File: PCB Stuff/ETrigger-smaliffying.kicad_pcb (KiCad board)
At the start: 2 copper layers, 33.7 x 27.5 mm, 53 parts, among them IC1 ATTINY85-S, P1 CONN_01X04, Q1 S8550, Q2 S8550, U1 AP1117, U4 LM321C

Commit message: Wow....
No comment I need to slow down a bit...and probably go to bed...
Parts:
- removed the REF** at (152.5, 90.8)
- removed the REF** at (151.5, 90.8)
- renumbered U4 to LM321, Q1 to S8550, Q2 to S8550, U1 to xx1117
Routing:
- net VCC_ICSP: track 140.6 -> 132.7 mm
- net GND_ICSP: track 56.4 -> 57.8 mm
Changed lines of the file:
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@@
 (kicad_pcb (version 4) (host pcbnew 4.0.5)
   (general
-    (links 82)
+    (links 0)
     (no_connects 0)
     (area 136.830709 82.456999 170.595002 111.507001)
     (thickness 1.6)
     (drawings 248)
-    (tracks 319)
+    (tracks 318)
     (zones 0)
-    (modules 53)
+    (modules 51)
     (nets 17)
   )
   (page A4)
   (layers
-    (0 F.Cu signal)
+    (0 F.Cu signal hide)
     (31 B.Cu signal)
     (32 B.Adhes user)
@@
     (visible_elements 7FFEF6FF)
     (pcbplotparams
-      (layerselection 0x00030_80000001)
-      (usegerberextensions false)
+      (layerselection 0x011f0_80000001)
+      (usegerberextensions true)
       (excludeedgelayer true)
       (linewidth 0.100000)
@@
       (outputformat 1)
       (mirror false)
-      (drillshape 1)
+      (drillshape 0)
       (scaleselection 1)
-      (outputdirectory ""))
+      (outputdirectory "ETrig Board/"))
   )
   (net 0 "")
@@
     (add_net VCC_ICSP)
   )
+  (module TO_SOT_Packages_SMD:SOT-223 (layer F.Cu)
+    (at 150.8379 89.0647 270)
+    (descr "module CMS SOT223 4 pins")
+    (tags "CMS SOT")
+    (attr smd)
+    (fp_text reference xx1117 (at 3.15 -3.5433 360) (layer F.SilkS)
+      (effects (font (size 0.5 0.5) (thickness 0.1)))
+    )
+    (fp_text value AP1117 (at 0 4.5 270) (layer F.Fab)
+      (effects (font (size 1 1) (thickness 0.15)))
+    )
+    (fp_text user %R (at 0 0 270) (layer F.Fab)
+      (effects (font (size 0.8 0.8) (thickness 0.12)))
+    )
+    (fp_line (start -1.85 -2.3) (end -0.8 -3.35) (layer F.Fab) (width 0.1))
+    (fp_line (start 4.4 -3.6) (end -4.4 -3.6) (layer F.CrtYd) (width 0.05))
+    (fp_line (start 4.4 3.6) (end 4.4 -3.6) (layer F.CrtYd) (width 0.05))
+    (fp_line (start -4.4 3.6) (end 4.4 3.6) (layer F.CrtYd) (width 0.05))
+    (fp_line (start -4.4 -3.6) (end -4.4 3.6) (layer F.CrtYd) (width 0.05))
+    (fp_line (start -1.85 -2.3) (end -1.85 3.35) (layer F.Fab) (width 0.1))
+    (fp_line (start -0.8 -3.35) (end 1.85 -3.35) (layer F.Fab) (width 0.1))
+    (fp_line (start -1.85 3.35) (end 1.85 3.35) (layer F.Fab) (width 0.1))
+    (fp_line (start 1.85 -3.35) (end 1.85 3.35) (layer F.Fab) (width 0.1))
+    (pad 4 smd rect (at 3.15 0 270) (size 2 3.8) (layers F.Cu F.Paste F.Mask)
+      (net 1 VCC_ICSP) (zone_connect 2))
+    (pad 2 smd rect (at -3.15 0 270) (size 2 1.5) (layers F.Cu F.Paste F.Mask)
+      (net 1 VCC_ICSP))
+    (pad 3 smd rect (at -3.15 2.3 270) (size 2 1.5) (layers F.Cu F.Paste F.Mask)
+      (net 4 +BATT))
+    (pad 1 smd rect (at -3.15 -2.3 270) (size 2 1.5) (layers F.Cu F.Paste F.Mask)
+      (net 5 GND_ICSP))
+    (model ${KISYS3DMOD}/TO_SOT_Packages_SMD.3dshapes/SOT-223.wrl
+      (at (xyz 0 0 0))
+      (scale (xyz 0.5 0.5 0.5))
+      (rotate (xyz 0 0 90))
+    )
+  )
   (module Capacitors_SMD:C_0805_HandSoldering (layer F.Cu)
     (at 169.01 97.39 270)
@@
   )
   (module "Via 2" (layer F.Cu)
-    (at 152.47 90.78)
-    (clearance 0.00001)
-    (zone_connect 2)
-    (fp_text reference REF** (at 0.127 4.699) (layer F.SilkS) hide
-      (effects (font (size 0.127 0.127) (thickness 0.03175)))
-    )
-    (fp_text value "Via 2" (at -0.127 -5.969) (layer F.Fab) hide
-      (effects (font (size 0.127 0.127) (thickness 0.03175)))
-    )
-    (pad 1 thru_hole circle (at 0 0) (size 0.6 0.6) (drill 0.3) (layers *.Cu)
-      (net 1 VCC_ICSP) (zone_connect 2))
-  )
-  (module "Via 2" (layer F.Cu)
-    (at 151.47 90.78)
-    (clearance 0.00001)
-    (zone_connect 2)
-    (fp_text reference REF** (at 0.127 4.699) (layer F.SilkS) hide
-      (effects (font (size 0.127 0.127) (thickness 0.03175)))
-    )
-    (fp_text value "Via 2" (at -0.127 -5.969) (layer F.Fab) hide
-      (effects (font (size 0.127 0.127) (thickness 0.03175)))
-    )
-    (pad 1 thru_hole circle (at 0 0) (size 0.6 0.6) (drill 0.3) (layers *.Cu)
-      (net 1 VCC_ICSP) (zone_connect 2))
-  )
-  (module "Via 2" (layer F.Cu)
     (at 152.47 90.03)
     (clearance 0.00001)
@@
     (pad 1 thru_hole circle (at 0 0) (size 0.6 0.6) (drill 0.3) (layers *.Cu)
       (net 5 GND_ICSP) (zone_connect 2))
-  )
-  (module TO_SOT_Packages_SMD:SOT-223 (layer F.Cu)
-    (at 150.8379 89.0774 270)
-    (descr "module CMS SOT223 4 pins")
-    (tags "CMS SOT")
-    (attr smd)
-    (fp_text reference U1 (at 3.0611 -2.9591 360) (layer F.SilkS)
-      (effects (font (size 1 1) (thickness 0.15)))
-    )
-    (fp_text value AP1117 (at 0 4.5 270) (layer F.Fab)
-      (effects (font (size 1 1) (thickness 0.15)))
-    )
-    (fp_text user %R (at 0 0 270) (layer F.Fab)
-      (effects (font (size 0.8 0.8) (thickness 0.12)))
-    )
-    (fp_line (start -1.85 -2.3) (end -0.8 -3.35) (layer F.Fab) (width 0.1))
-    (fp_line (start 4.4 -3.6) (end -4.4 -3.6) (layer F.CrtYd) (width 0.05))
-    (fp_line (start 4.4 3.6) (end 4.4 -3.6) (layer F.CrtYd) (width 0.05))
-    (fp_line (start -4.4 3.6) (end 4.4 3.6) (layer F.CrtYd) (width 0.05))
-    (fp_line (start -4.4 -3.6) (end -4.4 3.6) (layer F.CrtYd) (width 0.05))
-    (fp_line (start -1.85 -2.3) (end -1.85 3.35) (layer F.Fab) (width 0.1))
-    (fp_line (start -0.8 -3.35) (end 1.85 -3.35) (layer F.Fab) (width 0.1))
-    (fp_line (start -1.85 3.35) (end 1.85 3.35) (layer F.Fab) (width 0.1))
-    (fp_line (start 1.85 -3.35) (end 1.85 3.35) (layer F.Fab) (width 0.1))
-    (pad 4 smd rect (at 3.15 0 270) (size 2 3.8) (layers F.Cu F.Paste)
-      (net 1 VCC_ICSP) (zone_connect 2))
-    (pad 2 smd rect (at -3.15 0 270) (size 2 1.5) (layers F.Cu F.Paste)
-      (net 1 VCC_ICSP))
-    (pad 3 smd rect (at -3.15 2.3 270) (size 2 1.5) (layers F.Cu F.Paste)
-      (net 4 +BATT))
-    (pad 1 smd rect (at -3.15 -2.3 270) (size 2 1.5) (layers F.Cu F.Paste)
-      (net 5 GND_ICSP))
-    (model ${KISYS3DMOD}/TO_SOT_Packages_SMD.3dshapes/SOT-223.wrl
-      (at (xyz 0 0 0))
-      (scale (xyz 0.5 0.5 0.5))
-      (rotate (xyz 0 0 90))
-    )
   )
   (module Via (layer F.Cu)
@@
     (tags "SOT-23-5 hand-soldering")
     (attr smd)
-    (fp_text reference U4 (at 0 -2.9 270) (layer F.SilkS)
+    (fp_text reference LM321 (at 0 -2.9 270) (layer F.SilkS)
       (effects (font (size 1 1) (thickness 0.15)))
     )
@@
     (tags SOT-23)
     (attr smd)
-    (fp_text reference Q1 (at 0 -2.5 180) (layer F.SilkS) hide
-      (effects (font (size 1 1) (thickness 0.15)))
+    (fp_text reference S8550 (at 0.5955 2.13614 180) (layer F.SilkS)
+      (effects (font (size 0.5 0.5) (thickness 0.1)))
     )
     (fp_text value S8550 (at 0 2.5 180) (layer F.Fab)
@@
       (at (xyz 0 0 0))
       (scale (xyz 1 1 1))
-      (rotate (xyz 0 0 0))
+      (rotate (xyz 0 0 90))
     )
   )
@@
     (tags SOT-23)
     (attr smd)
-    (fp_text reference Q2 (at -0.3738 2.51978) (layer F.SilkS)
-      (effects (font (size 1 1) (thickness 0.15)))
+    (fp_text reference S8550 (at -1.4859 2.16408) (layer F.SilkS)
+      (effects (font (size 0.5 0.5) (thickness 0.1)))
     )
     (fp_text value S8550 (at 0 2.5) (layer F.Fab)
@@
       (at (xyz 0 0 0))
       (scale (xyz 1 1 1))
-      (rotate (xyz 0 0 0))
+      (rotate (xyz 0 0 90))
     )
   )
@@
     (tags "Mesurement Point Round SMD Pad 1.5mm")
     (attr virtual)
-    (fp_text reference W4 (at 0.04 -2.78) (layer B.SilkS)
+    (fp_text reference W4 (at 0.1091 -1.7617) (layer B.SilkS)
       (effects (font (size 1 1) (thickness 0.15)) (justify mirror))
     )
@@
   (via (at 162.4 95.9) (size 0.7) (drill 0.6) (layers F.Cu B.Cu) (net 1))
   (segment (start 162.2548 95.9) (end 162.4 95.9) (width 0.55) (layer F.Cu) (net 1))
-  (segment (start 159.745317 106.379917) (end 158.0134 104.648) (width 0.55) (layer B.Cu) (net 1))
-  (segment (start 163.688283 106.379917) (end 159.745317 106.379917) (width 0.55) (layer B.Cu) (net 1))
-  (segment (start 163.8554 106.2128) (end 163.688283 106.379917) (width 0.55) (layer B.Cu) (net 1))
-  (segment (start 163.8554 104.9128) (end 163.8554 106.2128) (width 0.55) (layer B.Cu) (net 1))
   (segment (start 137.7 96.26) (end 137.7 97.55) (width 0.55) (layer F.Cu) (net 1))
   (segment (start 137.74 96.22) (end 137.7 96.26) (width 0.55) (layer F.Cu) (net 1))
@@
   (via (at 144.966145 85.934137) (size 0.7) (drill 0.6) (layers F.Cu B.Cu) (net 4))
   (via (at 148.463 95.758) (size 0.7) (drill 0.6) (layers F.Cu B.Cu) (net 4))
+  (segment (start 158.3309 106.9086) (end 158.7627 106.4768) (width 0.25) (layer B.Cu) (net 5))
+  (segment (start 158.3309 106.9975) (end 158.3309 106.9086) (width 0.25) (layer B.Cu) (net 5))
+  (segment (start 158.3309 107.3765) (end 158.3309 106.9975) (width 0.25) (layer B.Cu) (net 5))
+  (segment (start 159.6688 107.7644) (end 158.7188 107.7644) (width 0.25) (layer B.Cu) (net 5))
+  (segment (start 158.7188 107.7644) (end 158.3309 107.3765) (width 0.25) (layer B.Cu) (net 5))
   (segment (start 152.673615 85.835353) (end 153.097879 85.835353) (width 0.25) (layer F.Cu) (net 5))
   (segment (start 152.654847 85.835353) (end 152.673615 85.835353) (width 0.25) (layer F.Cu) (net 5))
@@
   (segment (start 151.5618 102.6668) (end 151.541135 102.646135) (width 0.25) (layer F.Cu) (net 5))
   (via (at 151.541135 100.983493) (size 0.6) (drill 0.4) (layers F.Cu B.Cu) (net 5))
-  (segment (start 158.7726 107.19304) (end 159.09744 107.19304) (width 0.25) (layer B.Cu) (net 5))
-  (segment (start 159.09744 107.19304) (end 159.6688 107.7644) (width 0.25) (layer B.Cu) (net 5))
   (via (at 139.3938 85.90022) (size 0.6) (drill 0.4) (layers F.Cu B.Cu) (net 5))
   (via (at 151.0636 97.6122) (size 0.6) (drill 0.4) (layers F.Cu B.Cu) (net 5))
@@
       )
     )
-  )
-  (zone (net 0) (net_name "") (layer F.Mask) (hatch edge 0.508)
-    (connect_pads (clearance 0.508))
-    (min_thickness 0.254)
-    (fill yes (arc_segments 16) (thermal_gap 0.508) (thermal_bridge_width 0.508))
-    (polygon
-      (pts
-        (xy 147.32 91.059) (xy 147.32 87.122) (xy 154.305 87.122) (xy 154.305 91.059)
-      )
-    )

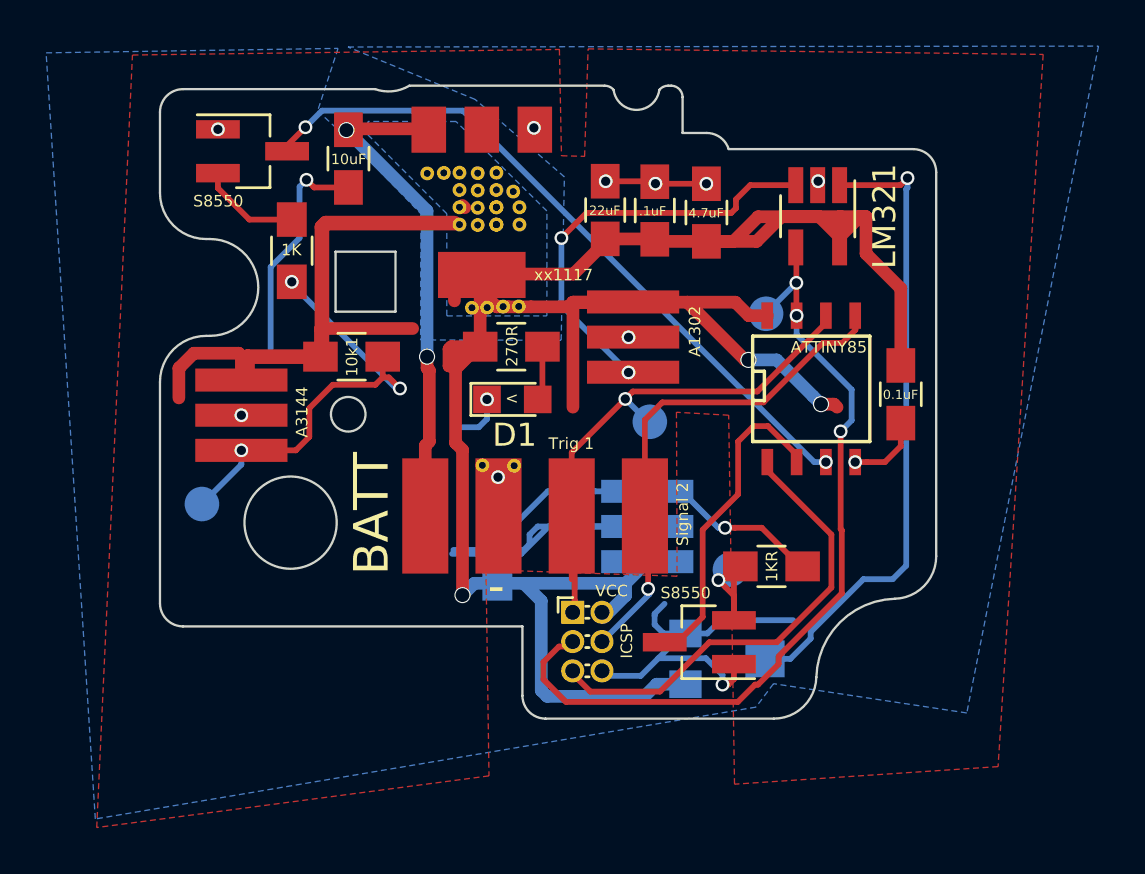
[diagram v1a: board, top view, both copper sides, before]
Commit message: Quick PCB update
Added resistors to outputs on attiny to avoid over current, either into
a mosfet or mosfet driver
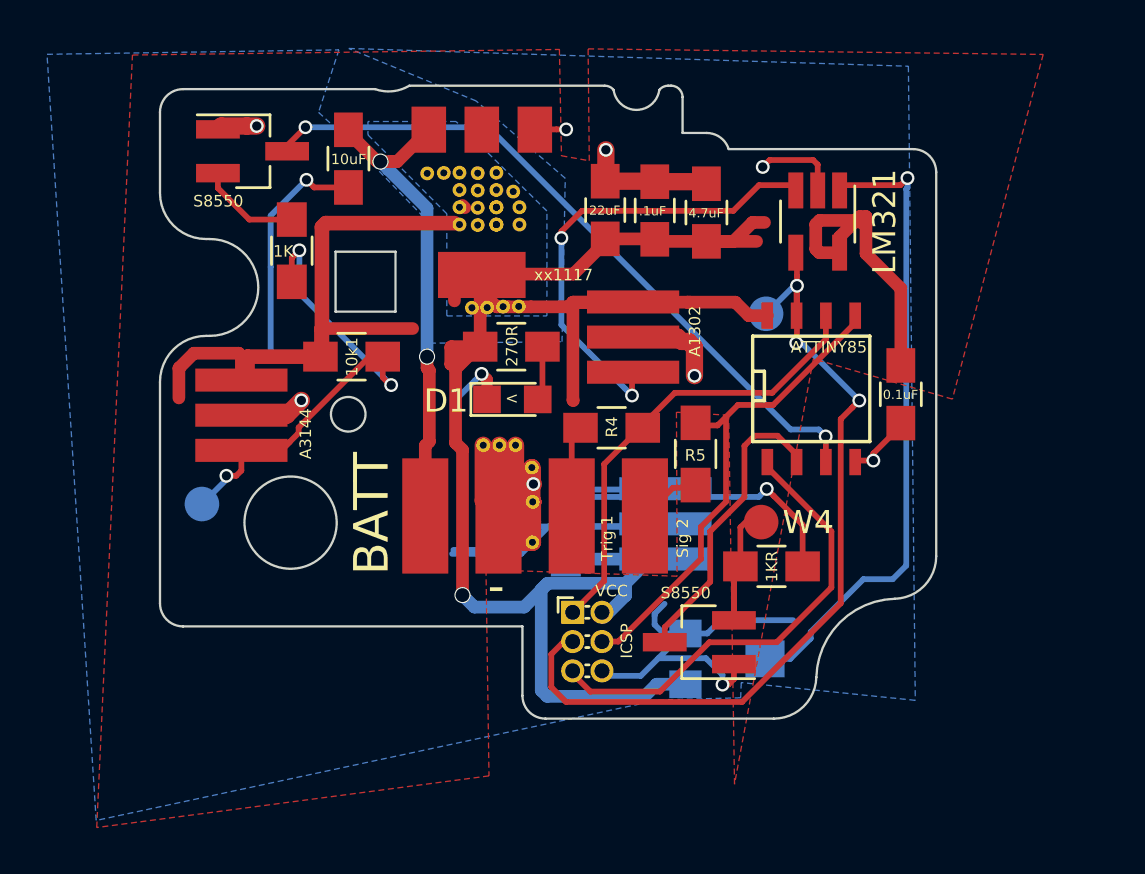
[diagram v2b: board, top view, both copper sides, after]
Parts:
- removed W3: TEST_1P, Measurement_Points:Measurement_Point_Round-SMD-Pad_Small
- added R4: R, Resistors_SMD:R_0805_HandSoldering, F.Cu at (156.5, 98.8)
- added R5: R, Resistors_SMD:R_0805_HandSoldering, F.Cu at (160.1, 100.0)
- added REF**: Via, Via, F.Cu at (152.3, 99.6)
- added REF**: Via, Via, F.Cu at (153.0, 102.1)
- added REF**: Via, Via, F.Cu at (153.0, 103.8)
- added REF**: Via, Via, F.Cu at (151.6, 99.6)
- W4: moved to F.Cu
- moved 10k 3.15 mm to (154.5, 103.2)
- moved W4 2.47 mm to (163.0, 102.9)
- moved REF** 0.87 mm to (150.9, 99.6)
- moved A3144 0.80 mm to (158.8, 105.3)
- moved REF** 0.77 mm to (153.0, 100.6)
- moved LM321 0.23 mm to (165.4, 89.9)
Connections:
- IC1 pad 5: OutTrig2 -> Net-(IC1-Pad5)
- ICSP pad 4: OutTrig2 -> Net-(IC1-Pad5)
- P1 pad 2: MISO_ICSP -> OutTrig
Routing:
- net GND_ICSP: track 57.8 -> 101.4 mm, vias 13 -> 11
- net Net-(IC1-Pad5): track 0.00 -> 21.4 mm
- net OutTrig2: track 21.9 -> 2.76 mm, vias 1 -> 0
- net VCC_ICSP: track 132.7 -> 122.0 mm, vias 3 -> 1
- net OutTrig: track 0.00 -> 5.66 mm
- net MISO_ICSP: track 25.8 -> 20.3 mm, vias 1 -> 0
- net Net-(10k2-Pad2): track 15.1 -> 17.3 mm
- net Net-(10k1-Pad2): track 19.7 -> 21.9 mm
- net Net-(IC2-Pad3): track 18.4 -> 20.4 mm
- net Net-(Q1-Pad2): track 5.16 -> 7.09 mm, vias 1 -> 0
- net InTrig: track 35.6 -> 36.9 mm
- net Net-(IC1-Pad2): track 14.3 -> 13.1 mm
- net +BATT: track 21.9 -> 21.0 mm
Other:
- net class GND added: clearance 0.1524, trace_width 0.75, via_dia 0.6, via_drill 0.4
- board text added: "Sig 2"
- board text removed: "Signal 2"
